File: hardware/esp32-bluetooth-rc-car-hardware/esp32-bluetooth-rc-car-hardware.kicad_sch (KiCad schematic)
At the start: 0 parts

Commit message: create ESP32 RC Car schematic
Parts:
- added BT1: Battery, symbol Device:Battery
- added M1, M2: Motor_DC, symbol Motor:Motor_DC
- added U1: ESP32_DevKit_V1, symbol ESP32_devkit_v1:ESP32_DevKit_V1
- added U2: TB503A16612FNG, symbol h_bridge_steering_car:Pololu_MD08A07303
- added U3: LM2596, symbol buck_converter:LM2596
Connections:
- new net: U1.6 (GPIO16), U2.10 (PWMB)
- new net: U1.13 (GPIO1), U2.11 (BIN2)
- new net: U1.12 (GPIO3), U2.12 (BIN1)
- new net: U1.7 (GPIO17), U2.14 (AIN1)
- new net: U1.6 (GPIO16), U2.15 (AIN2)
- new net: U1.9 (GPIO18), U2.16 (PWMA)
- new net: BT1.1 (+), U2.2 (VMOT), U3.1 (VIN_P)
- new net: M1.1 (+), U2.3 (BO1)
- new net: M1.2 (-), U2.4 (BO2)
- new net: M2.2 (-), U2.5 (AO2)
- new net: M2.1 (+), U2.6 (AO1)
- new net: U1.1 (3.3V), U2.7 (VCC)
- new net: U1.2 (GND), U2.9 (GND)
- new net: U1.1 (3.3V), U3.2 (VOUT_P)
- new net: U1.2 (GND), U3.2 (VOUT_P)
- new net GND: BT1.2 (-), U2.1 (GND), U3.1 (VIN_P)
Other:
- note added: "+7.4V (nominal)"
- note added: "1 channel = 1A 2 channels = 2A"
- note added: "2 li-ion batteries = 7.4V nominal"
- note added: "V output = 5"
- note added: "boot*"

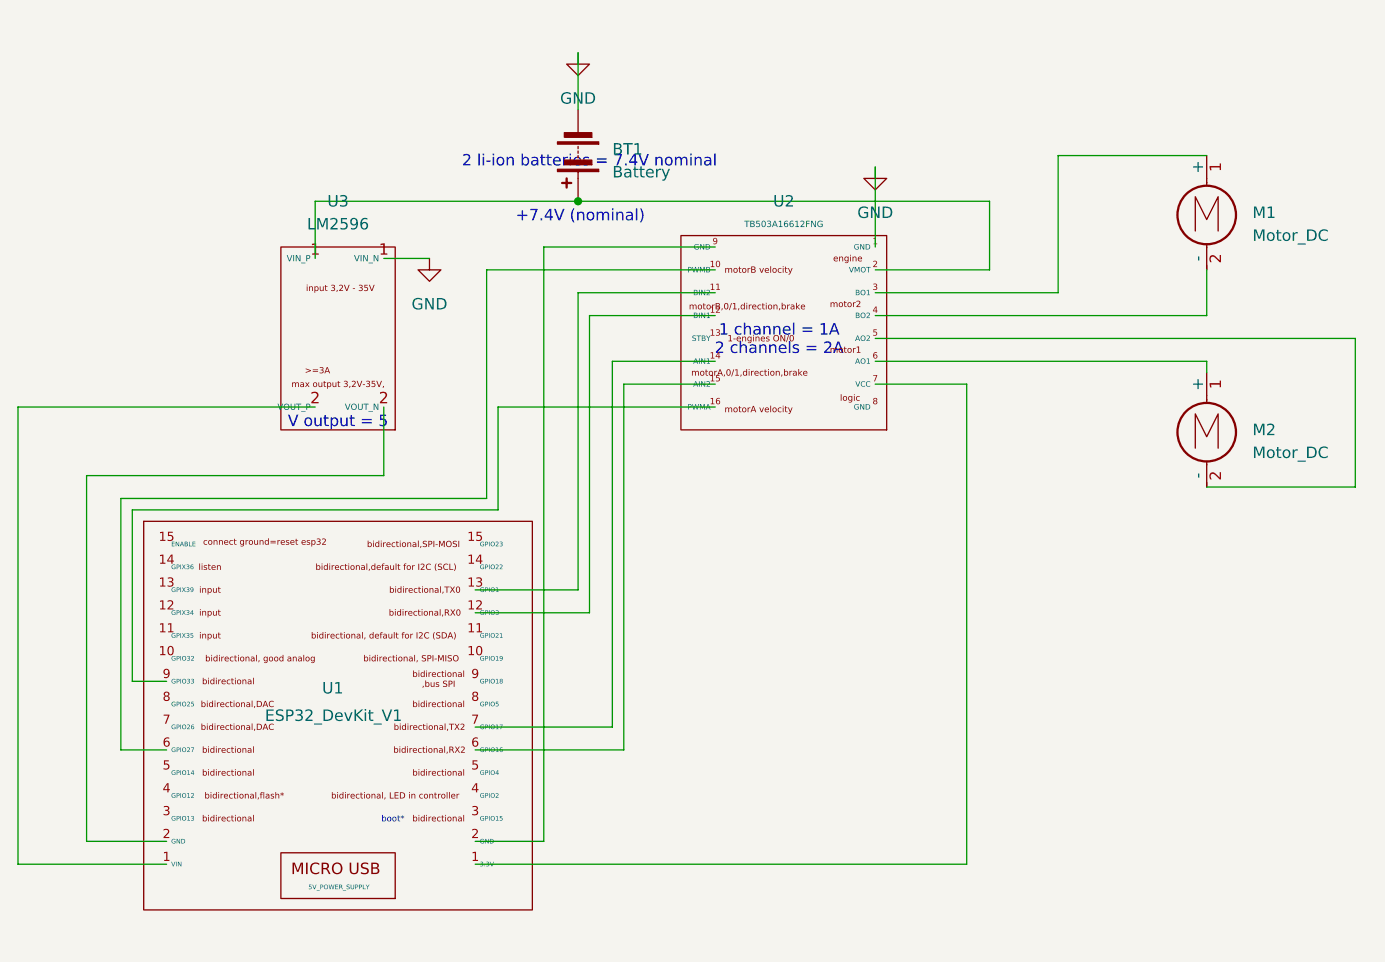
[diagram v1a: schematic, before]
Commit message: add switch-button for power line
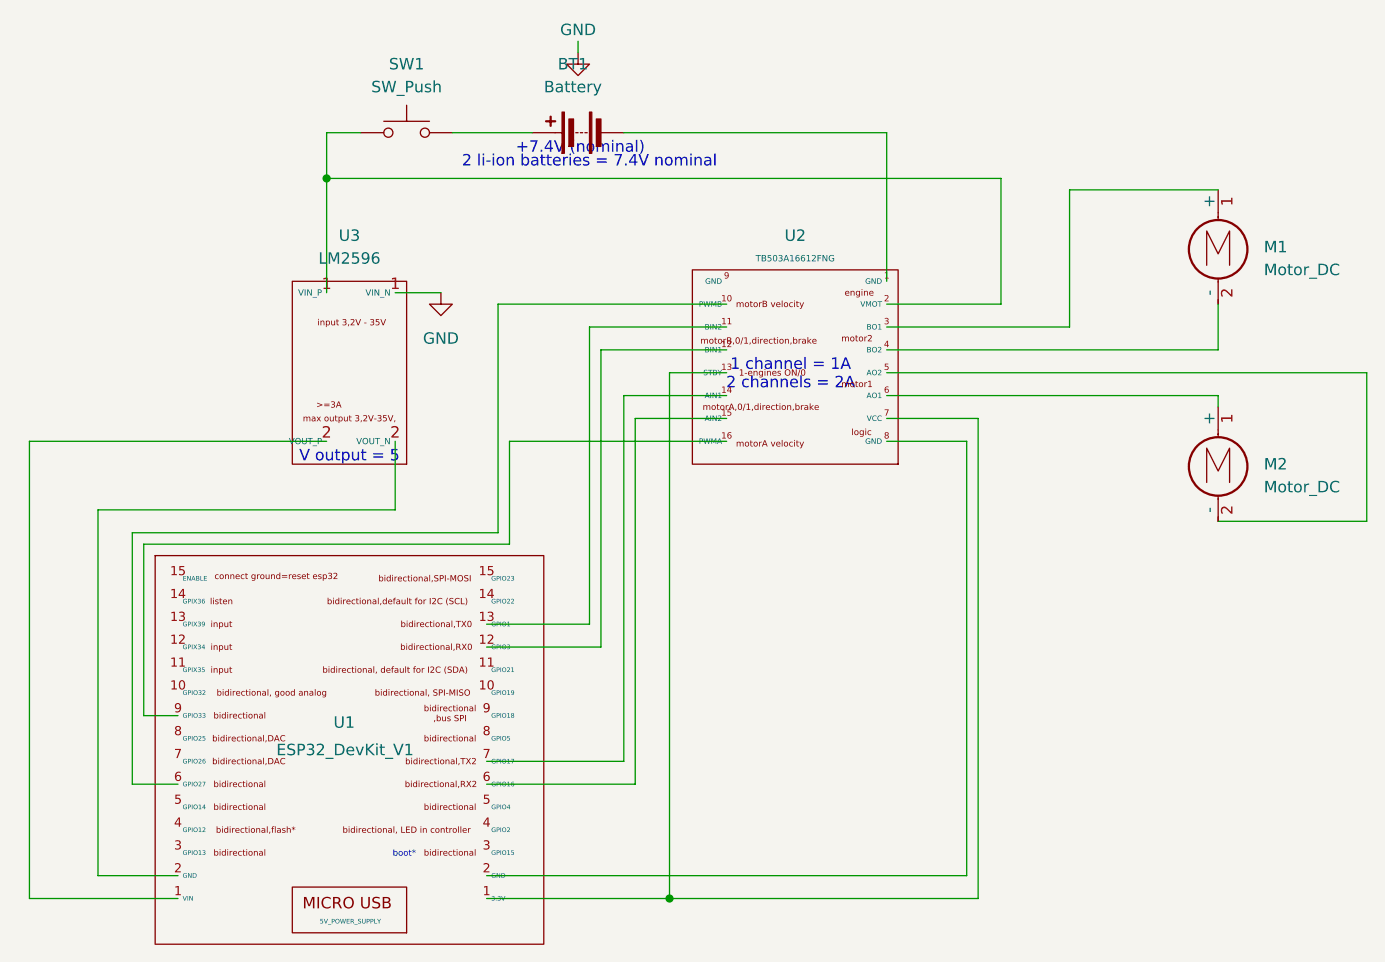
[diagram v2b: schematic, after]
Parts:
- added SW1: SW_Push, symbol Switch:SW_Push
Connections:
- net GND: no longer BT1.2 (-), U2.1 (GND)
- net at U2.13 (STBY): now also U1.1 (3.3V), U2.7 (VCC)
- net at U1.1 (3.3V): now also U3.2 (VOUT_P); no longer U2.7 (VCC)
- net at U2.8 (GND): now also U1.2 (GND)
- net at U2.9 (GND): no longer U1.2 (GND)
- net at U3.2 (VOUT_P): now also U1.2 (GND); no longer U1.1 (3.3V)
- new net: BT1.2 (-), U2.1 (GND)
- new net: SW1.1, U2.2 (VMOT), U3.1 (VIN_P)
- new net: BT1.1 (+), SW1.2
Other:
- moved on the sheet: BT1, M1, M2, U1, U2, U3

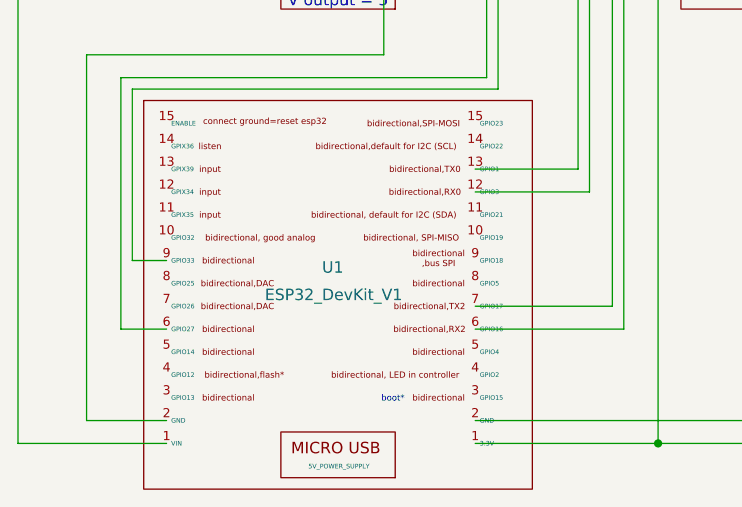
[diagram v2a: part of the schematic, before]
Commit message: update project schematic of updated esp32 symbol schematic
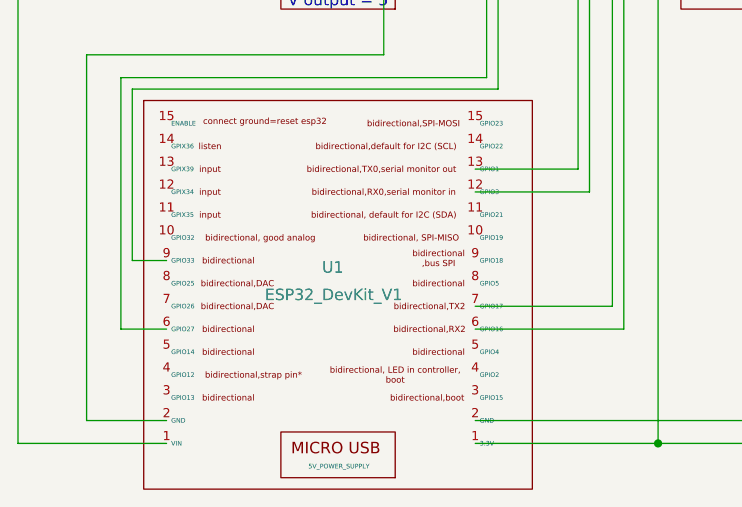
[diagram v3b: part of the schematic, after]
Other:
- note removed: "boot*"
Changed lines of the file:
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@@
-		)
-	)
-	(text "boot*"
-		(exclude_from_sim no)
-		(at 114.046 106.934 0)
-		(effects
-			(font
-				(size 0.6858 0.6858)
-			)
 		)
 	)

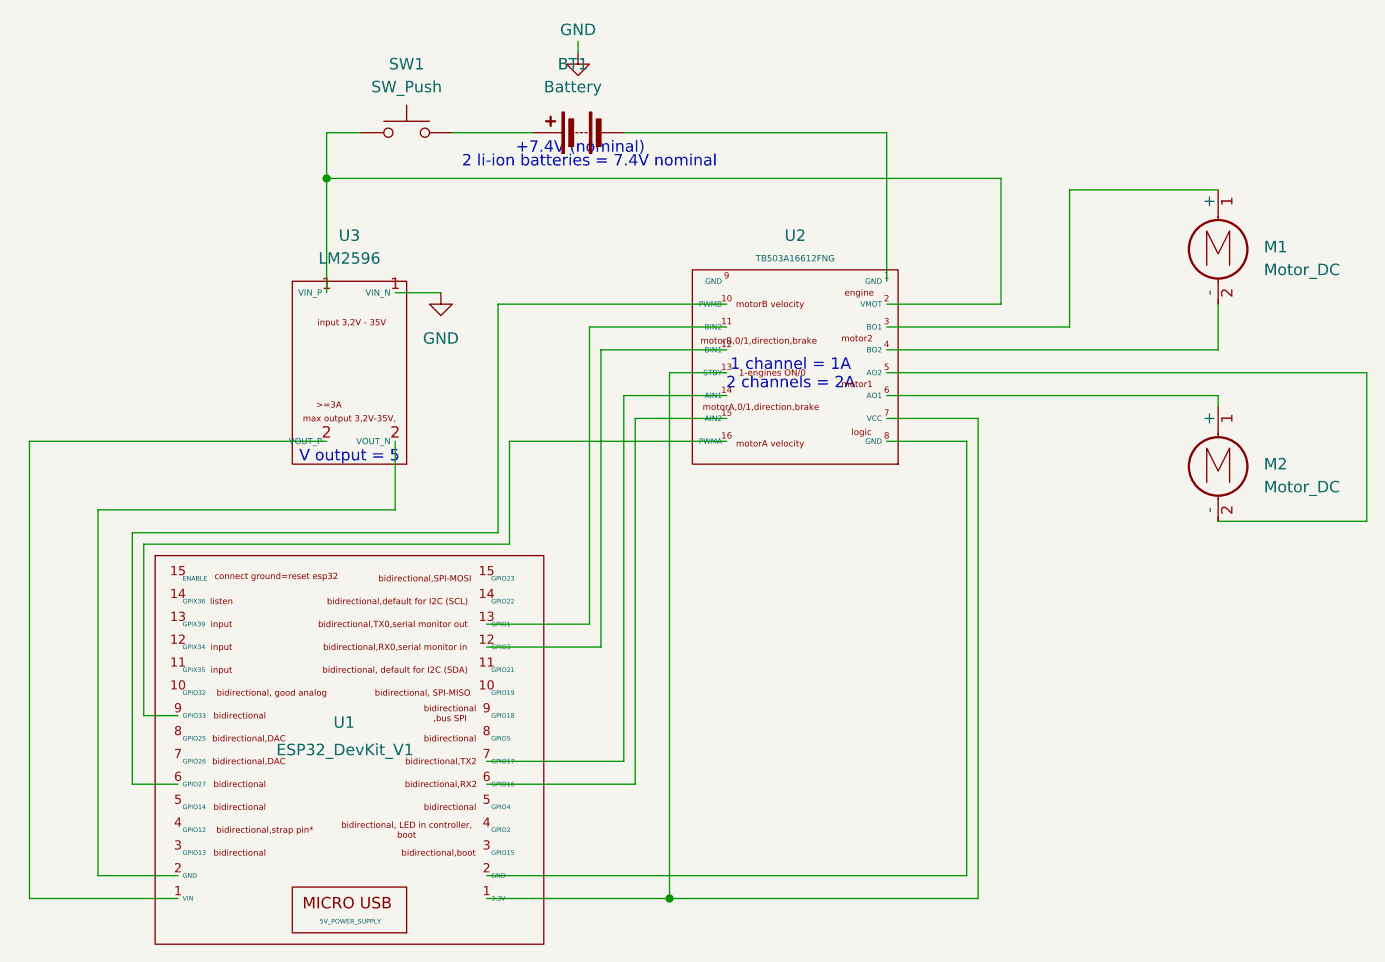
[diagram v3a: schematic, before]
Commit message: changed connections for right wheel and add standby connection
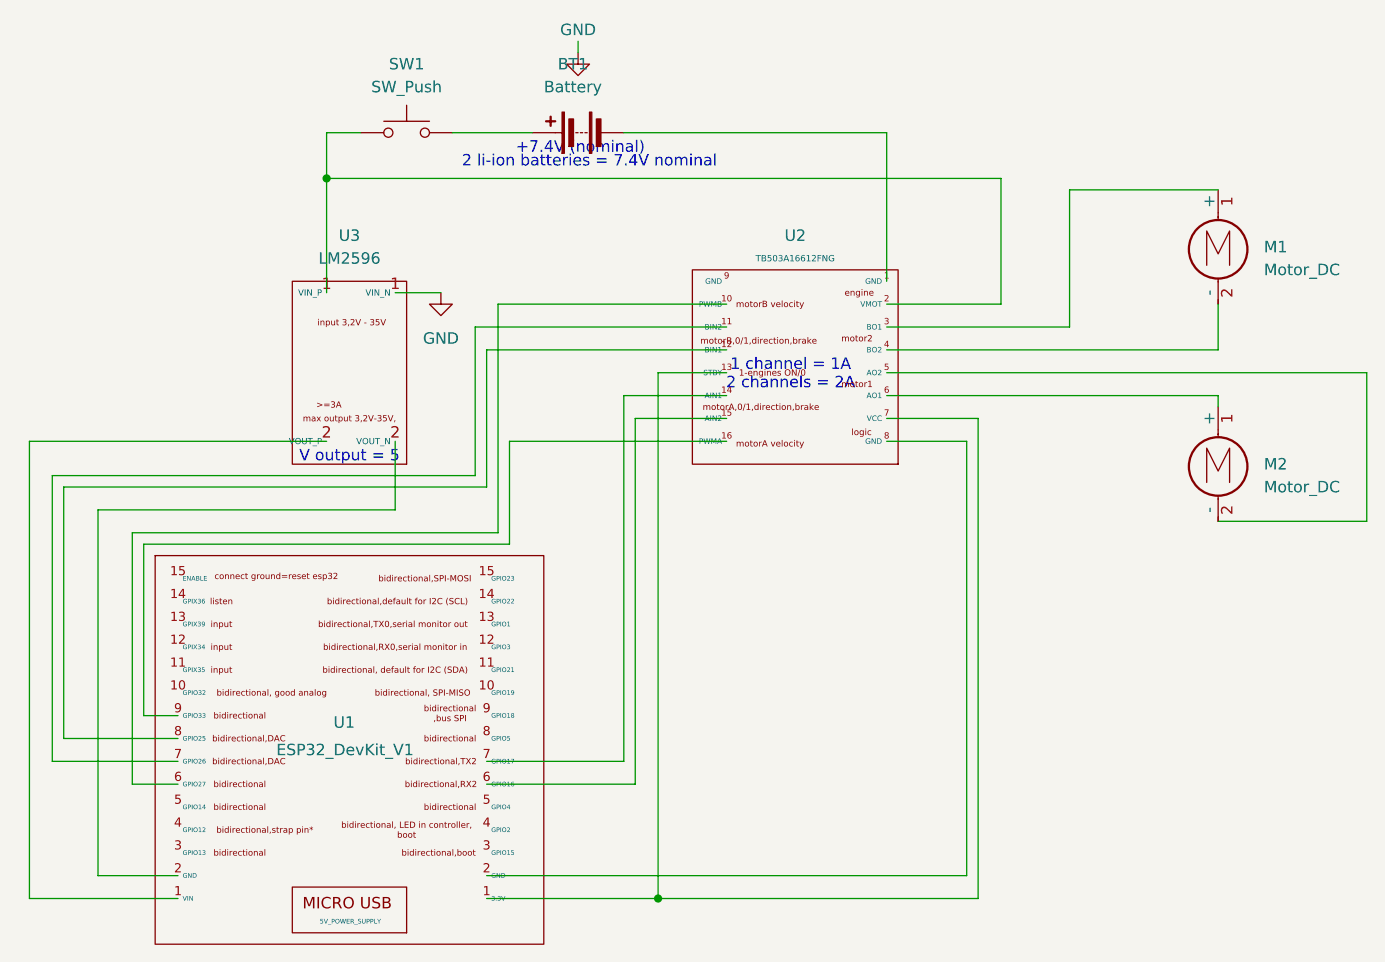
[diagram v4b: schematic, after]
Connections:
- net at U2.11 (BIN2): now also U1.7 (GPIO17); no longer U1.13 (GPIO1)
- net at U2.12 (BIN1): now also U1.8 (GPIO5); no longer U1.12 (GPIO3)
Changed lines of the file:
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@@
 	)
 	(junction
-		(at 143.51 111.76)
+		(at 142.24 111.76)
 		(diameter 0)
 		(color 0 0 0 0)
@@
 	(wire
 		(pts
-			(xy 149.86 53.34) (xy 143.51 53.34)
+			(xy 149.86 53.34) (xy 142.24 53.34)
 		)
 		(stroke
@@
 	(wire
 		(pts
-			(xy 135.89 83.82) (xy 135.89 50.8)
-		)
-		(stroke
-			(width 0)
-			(type default)
-		)
-	)
-	(wire
-		(pts
 			(xy 176.53 109.22) (xy 176.53 60.96)
 		)
@@
 	(wire
 		(pts
+			(xy 76.2 93.98) (xy 76.2 66.04)
+		)
+		(stroke
+			(width 0)
+			(type default)
+		)
+	)
+	(wire
+		(pts
 			(xy 119.38 26.67) (xy 128.27 26.67)
 		)
@@
 	(wire
 		(pts
+			(xy 76.2 66.04) (xy 123.19 66.04)
+		)
+		(stroke
+			(width 0)
+			(type default)
+		)
+	)
+	(wire
+		(pts
 			(xy 113.03 44.45) (xy 118.11 44.45)
 		)
@@
 	(wire
 		(pts
-			(xy 143.51 53.34) (xy 143.51 111.76)
+			(xy 123.19 50.8) (xy 149.86 50.8)
+		)
+		(stroke
+			(width 0)
+			(type default)
+		)
+	)
+	(wire
+		(pts
+			(xy 142.24 53.34) (xy 142.24 111.76)
+		)
+		(stroke
+			(width 0)
+			(type default)
+		)
+	)
+	(wire
+		(pts
+			(xy 123.19 66.04) (xy 123.19 50.8)
 		)
 		(stroke
@@
 	(wire
 		(pts
+			(xy 121.92 48.26) (xy 149.86 48.26)
+		)
+		(stroke
+			(width 0)
+			(type default)
+		)
+	)
+	(wire
+		(pts
 			(xy 167.64 53.34) (xy 220.98 53.34)
 		)
@@
 	(wire
 		(pts
-			(xy 134.62 48.26) (xy 149.86 48.26)
-		)
-		(stroke
-			(width 0)
-			(type default)
-		)
-	)
-	(wire
-		(pts
-			(xy 123.19 81.28) (xy 134.62 81.28)
-		)
-		(stroke
-			(width 0)
-			(type default)
-		)
-	)
-	(wire
-		(pts
-			(xy 135.89 50.8) (xy 149.86 50.8)
+			(xy 142.24 111.76) (xy 177.8 111.76)
 		)
 		(stroke
@@
 	(wire
 		(pts
-			(xy 143.51 111.76) (xy 177.8 111.76)
+			(xy 88.9 96.52) (xy 74.93 96.52)
 		)
 		(stroke
@@
 	(wire
 		(pts
-			(xy 123.19 111.76) (xy 143.51 111.76)
+			(xy 121.92 64.77) (xy 121.92 48.26)
+		)
+		(stroke
+			(width 0)
+			(type default)
+		)
+	)
+	(wire
+		(pts
+			(xy 123.19 111.76) (xy 142.24 111.76)
 		)
 		(stroke
@@
 	(wire
 		(pts
-			(xy 134.62 81.28) (xy 134.62 48.26)
+			(xy 74.93 96.52) (xy 74.93 64.77)
 		)
 		(stroke
@@
 	(wire
 		(pts
+			(xy 88.9 93.98) (xy 76.2 93.98)
+		)
+		(stroke
+			(width 0)
+			(type default)
+		)
+	)
+	(wire
+		(pts
 			(xy 124.46 45.72) (xy 149.86 45.72)
 		)
@@
 	(wire
 		(pts
-			(xy 123.19 83.82) (xy 135.89 83.82)
-		)
-		(stroke
-			(width 0)
-			(type default)
-		)
-	)
-	(wire
-		(pts
 			(xy 125.73 72.39) (xy 125.73 60.96)
 		)
@@
 		)
 		(stroke
+			(width 0)
+			(type default)
+		)
+	)
+	(wire
+		(pts
+			(xy 74.93 64.77) (xy 121.92 64.77)
+		)
+		(stroke
